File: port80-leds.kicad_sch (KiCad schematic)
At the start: 0 parts

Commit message: [#103224] Add 7-segment display section, add battery cicruit
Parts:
- added C6001, C6002, C6003, C6004, C6005, C6006, C6007, C6008: C_100n_0402, antmicro-footprints:C_0402_1005Metric, symbol Capacitors0402:C_100n_0402
- added D6001: ACDA02-41SURKWA-F01, antmicro-footprints:ACDA02-41SURKWA-F01, symbol Antmicro Symbols:ACDA02-41SURKWA-F01
- added R6001, R6002, R6003, R6004, R6005, R6006, R6007, R6008, R6009, R6010, R6011, R6012, R6013, R6014, R6015, R6016: R_200R_0402, antmicro-footprints:R_0402_1005Metric, symbol Antmicro Symbols:R_200R_0402
- added U6001, U6002, U6003, U6004, U6005, U6006, U6007, U6008: SN74LVC2G07DCKR, antmicro-footprints:SC-70-6, symbol LogicBuffersDriversReceiversTransceivers:SN74LVC2G07DCKR
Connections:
- new net: D6001.1 (E1), R6005.2
- new net: D6001.10 (DP2), R6009.2
- new net: D6001.11 (B2), R6015.2
- new net: D6001.12 (A2), R6016.2
- new net: D6001.14 (F2), R6011.2
- new net: D6001.15 (G2), R6010.2
- new net: D6001.16 (B1), R6002.2
- new net: D6001.17 (A1), R6001.2
- new net: D6001.19 (F1), R6006.2
- new net: D6001.2 (D1), R6004.2
- new net: D6001.20 (G1), R6007.2
- new net: D6001.4 (C1), R6003.2
- new net: D6001.5 (DP1), R6008.2
- new net: D6001.6 (E2), R6012.2
- new net: D6001.7 (D2), R6013.2
- new net: D6001.9 (C2), R6014.2
- new net: R6005.1, U6003.6 (1Y)
- new net: R6004.1, U6002.4 (2Y)
- new net: R6006.1, U6003.4 (2Y)
- new net: R6014.1, U6007.4 (2Y)
- new net: R6013.1, U6007.6 (1Y)
- new net: R6002.1, U6001.4 (2Y)
- new net: R6001.1, U6001.6 (1Y)
- new net: R6010.1, U6005.4 (2Y)
- new net: R6009.1, U6005.6 (1Y)
- new net: R6003.1, U6002.6 (1Y)
- new net: R6016.1, U6008.4 (2Y)
- new net: R6015.1, U6008.6 (1Y)
- new net: R6012.1, U6006.4 (2Y)
- new net: R6011.1, U6006.6 (1Y)
- new net: R6008.1, U6004.4 (2Y)
- new net: R6007.1, U6004.6 (1Y)
- new net +3.3V: C6001.1, C6002.1, C6003.1, C6004.1, C6005.1, C6006.1, C6007.1, C6008.1, D6001.[3,18] (COM1), D6001.[8,13] (COM2), U6001.5 (V_{CC}), U6002.5 (V_{CC}), U6003.5 (V_{CC}), U6004.5 (V_{CC}), U6005.5 (V_{CC}), U6006.5 (V_{CC}), U6007.5 (V_{CC}), U6008.5 (V_{CC})
- new net 7SEG_A1: U6001.1 (1A)
- new net 7SEG_A2: U6008.3 (2A)
- new net 7SEG_B1: U6001.3 (2A)
- new net 7SEG_B2: U6008.1 (1A)
- new net 7SEG_C1: U6002.1 (1A)
- new net 7SEG_C2: U6007.3 (2A)
- new net 7SEG_D1: U6002.3 (2A)
- new net 7SEG_D2: U6007.1 (1A)
- new net 7SEG_DP1: U6004.3 (2A)
- new net 7SEG_DP2: U6005.1 (1A)
- new net 7SEG_E1: U6003.1 (1A)
- new net 7SEG_E2: U6006.3 (2A)
- new net 7SEG_F1: U6003.3 (2A)
- new net 7SEG_F2: U6006.1 (1A)
- new net 7SEG_G1: U6004.1 (1A)
- new net 7SEG_G2: U6005.3 (2A)
- new net GND: C6001.2, C6002.2, C6003.2, C6004.2, C6005.2, C6006.2, C6007.2, C6008.2, U6001.2 (GND), U6002.2 (GND), U6003.2 (GND), U6004.2 (GND), U6005.2 (GND), U6006.2 (GND), U6007.2 (GND), U6008.2 (GND)
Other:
- note added: "Powered from 3.3V PIO registers set on drive strength - 8mA"

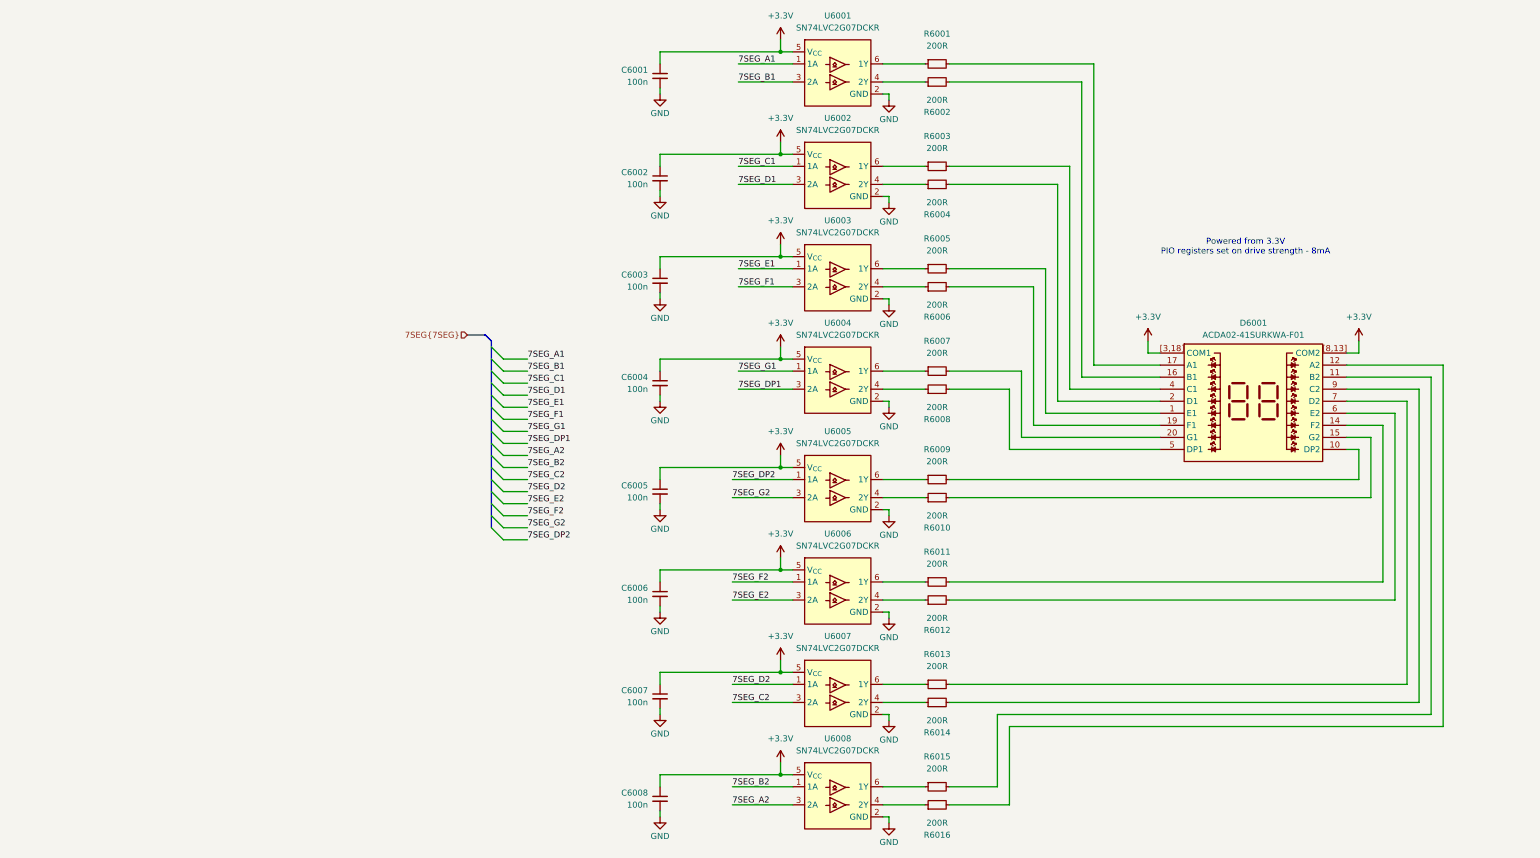
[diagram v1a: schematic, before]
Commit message: [#103224] Change buffer ICs, change JTAG connector, move BSS_STRAP resistors to MEC1723 sheet
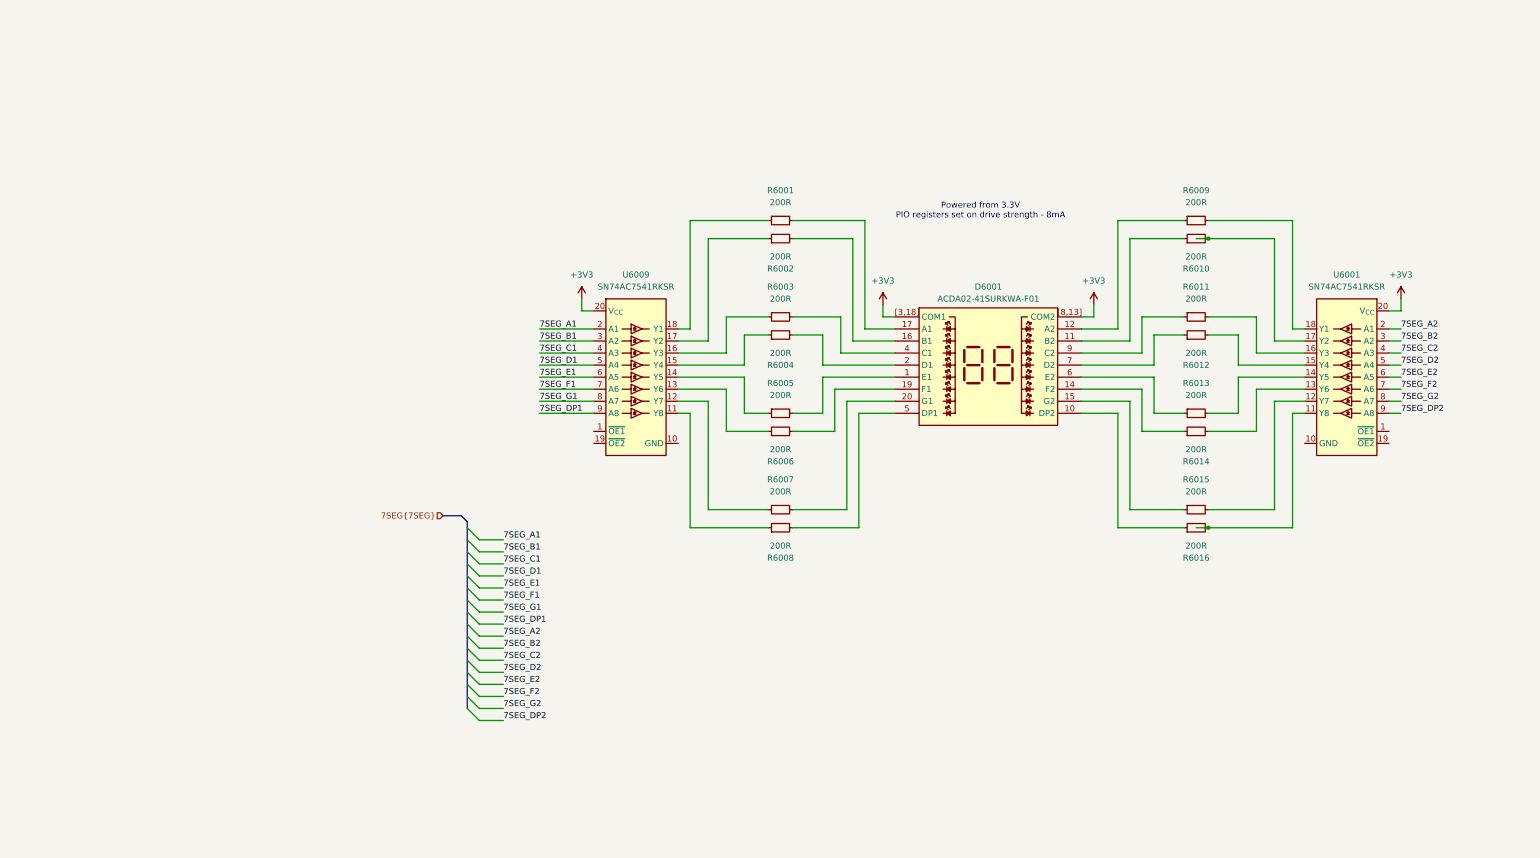
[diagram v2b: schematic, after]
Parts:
- removed C6001, C6002, C6003, C6004, C6005, C6006, C6007, C6008: C_100n_0402, antmicro-footprints:C_0402_1005Metric, symbol Capacitors0402:C_100n_0402
- removed U6001, U6002, U6003, U6004, U6005, U6006, U6007, U6008: SN74LVC2G07DCKR, antmicro-footprints:SC-70-6, symbol LogicBuffersDriversReceiversTransceivers:SN74LVC2G07DCKR
- added U6001, U6009: SN74AC7541_VQFN, antmicro-footprints:VQFN-20_1EP_4.5x2.5mm_P0.5mm, symbol Antmicro Symbols:SN74AC7541_VQFN
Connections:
- net 7SEG_A1: now also U6009.2 (A1)
- net 7SEG_A2: now also U6001.2 (A1)
- net 7SEG_B1: now also U6009.3 (A2)
- net 7SEG_B2: now also U6001.3 (A2)
- net 7SEG_C1: now also U6009.4 (A3)
- net 7SEG_C2: now also U6001.4 (A3)
- net 7SEG_D1: now also U6009.5 (A4)
- net 7SEG_D2: now also U6001.5 (A4)
- net 7SEG_DP1: now also U6009.9 (A8)
- net 7SEG_DP2: now also U6001.9 (A8)
- net 7SEG_E1: now also U6009.6 (A5)
- net 7SEG_E2: now also U6001.6 (A5)
- net 7SEG_F1: now also U6009.7 (A6)
- net 7SEG_F2: now also U6001.7 (A6)
- net 7SEG_G1: now also U6009.8 (A7)
- net 7SEG_G2: now also U6001.8 (A7)
- net at D6001.10 (DP2): now also R6016.1; no longer R6009.2
- net at D6001.11 (B2): now also R6010.1; no longer R6015.2
- net at D6001.12 (A2): now also R6009.1; no longer R6016.2
- net at D6001.14 (F2): now also R6014.1; no longer R6011.2
- net at D6001.15 (G2): now also R6015.1; no longer R6010.2
- net at D6001.6 (E2): now also R6013.1; no longer R6012.2
- net at D6001.7 (D2): now also R6012.1; no longer R6013.2
- net at D6001.9 (C2): now also R6011.1; no longer R6014.2
- net at R6005.1: now also U6009.14 (Y5)
- net at R6004.1: now also U6009.15 (Y4)
- net at R6006.1: now also U6009.13 (Y6)
- net at R6002.1: now also U6009.17 (Y2)
- net at R6001.1: now also U6009.18 (Y1)
- net at R6003.1: now also U6009.16 (Y3)
- net at R6008.1: now also U6009.11 (Y8)
- net at R6007.1: now also U6009.12 (Y7)
- net +3.3V renamed +3V3
- net +3V3: now also U6001.20 (V_{CC}), U6009.20 (V_{CC})
- new net: U6001.10 (GND), U6001.21 (GND)
- new net: R6016.2, U6001.11 (Y8)
- new net: R6015.2, U6001.12 (Y7)
- new net: R6014.2, U6001.13 (Y6)
- new net: R6013.2, U6001.14 (Y5)
- new net: R6012.2, U6001.15 (Y4)
- new net: R6011.2, U6001.16 (Y3)
- new net: R6010.2, U6001.17 (Y2)
- new net: R6009.2, U6001.18 (Y1)
- new net: U6009.10 (GND), U6009.21 (GND)
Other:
- moved on the sheet: D6001, R6001, R6002, R6003, R6004, R6005, R6006, R6007, R6008, R6009, R6010, R6011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

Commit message: [#103224] Route 7segment buffers, fix minor typos,add TODO list
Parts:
- added C6001, C6002: C_100n_0402, antmicro-footprints:C_0402_1005Metric, symbol Capacitors0402:C_100n_0402
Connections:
- net +3V3: now also C6001.1, C6002.1
- net 7SEG_~{OE1}_2: now reaches U6001.1 (~{OE1})
- net GND: now reaches U6001.10 (GND), U6001.21 (GND)
- net GND: now also U6009.10 (GND), U6009.21 (GND), C6001.2, C6002.2
- net 7SEG_~{OE2}_2: now reaches U6001.19 (~{OE2})
- net 7SEG_~{OE1}_1: now reaches U6009.1 (~{OE1})
- net 7SEG_~{OE2}_1: now reaches U6009.19 (~{OE2})
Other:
- moved on the sheet: U6001, U6009
